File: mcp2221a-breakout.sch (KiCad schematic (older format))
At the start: 27 parts, among them J1 USB_B_Micro, J2 LEFT, J3 RIGHT, U1 MCP1700-3302E, U2 MCP2221AxSL

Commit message: Switch regulator
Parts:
- removed U1: MCP1700-3302E, Package_TO_SOT_SMD:SOT-23, symbol Regulator_Linear:MCP1700-3302E_SOT23
- added U1: MCP1812AT-033_TT, Package_TO_SOT_SMD:SOT-23, symbol mcp2221a-breakout:MCP1812AT-033_TT
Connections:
- net GND: now also U1.3 (GND)
- net VBUS: now also U1.2 (VI)
- net VDD: now also U1.1 (VO)
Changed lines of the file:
@@
-$EndComp
-$Comp
-L Regulator_Linear:MCP1700-3302E_SOT23 U1
-U 1 1 60EED33E
-P 3650 1250
-F 0 "U1" H 3650 1492 50  0000 C CNN
-F 1 "MCP1700-3302E" H 3650 1401 50  0000 C CNN
-F 2 "Package_TO_SOT_SMD:SOT-23" H 3650 1475 50  0001 C CNN
-F 3 "http://ww1.microchip.com/downloads/en/DeviceDoc/20001826D.pdf" H 3650 1250 50  0001 C CNN
-	1    3650 1250
-	1    0    0    -1
 $EndComp
 $Comp
@@
 Wire Notes Line
 	4900 1950 4900 3800
+$Comp
+L mcp2221a-breakout:MCP1812AT-033_TT U1
+U 1 1 60F5FC01
+P 3650 1250
+F 0 "U1" H 3650 1492 50  0000 C CNN
+F 1 "MCP1812AT-033_TT" H 3650 1401 50  0000 C CNN
+F 2 "Package_TO_SOT_SMD:SOT-23" H 3650 1475 50  0001 C CNN
+F 3 "https://www.farnell.com/datasheets/2722379.pdf" H 3650 1250 50  0001 C CNN
+	1    3650 1250
+	1    0    0    -1
+$EndComp
 $EndSCHEMATC

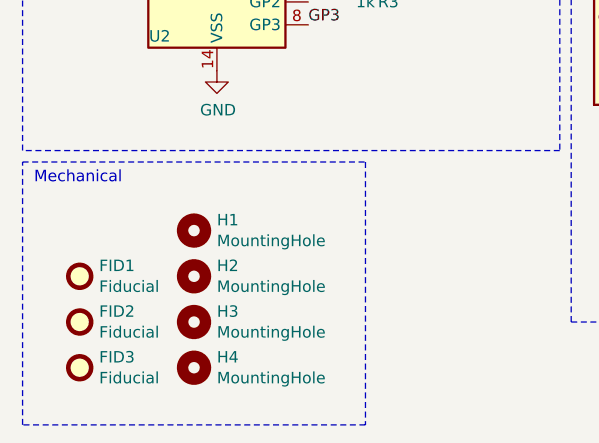
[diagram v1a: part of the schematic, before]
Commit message: Update for KICAD 6.0
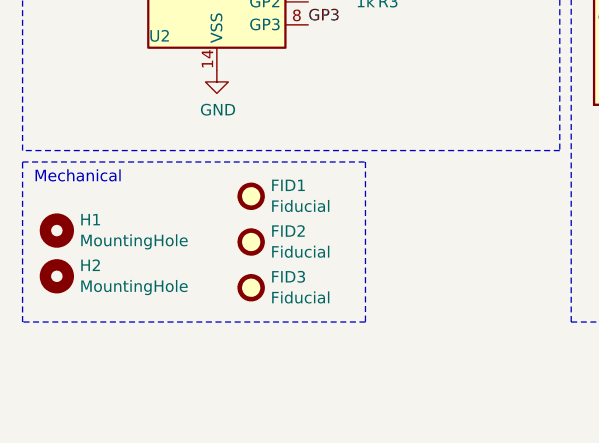
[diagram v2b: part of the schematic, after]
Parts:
- removed H3, H4: MountingHole, MountingHole:MountingHole_2.7mm_M2.5_DIN965_Pad, symbol Mechanical:MountingHole
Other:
- moved on the sheet: FID1, FID2, FID3, H1, H2
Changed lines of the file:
@@
 L Mechanical:Fiducial FID3
 U 1 1 60F19612
-P 750 4000
-F 0 "FID3" H 835 4046 50  0000 L CNN
-F 1 "Fiducial" H 835 3955 50  0000 L CNN
-F 2 "Fiducial:Fiducial_1mm_Mask2mm" H 750 4000 50  0001 C CNN
-F 3 "~" H 750 4000 50  0001 C CNN
-	1    750  4000
-	1    0    0    -1
-$EndComp
-$Comp
-L Mechanical:MountingHole H4
-U 1 1 60F1A4FC
-P 1250 4000
-F 0 "H4" H 1350 4046 50  0000 L CNN
-F 1 "MountingHole" H 1350 3955 50  0000 L CNN
-F 2 "MountingHole:MountingHole_2.7mm_M2.5_DIN965_Pad" H 1250 4000 50  0001 C CNN
-F 3 "~" H 1250 4000 50  0001 C CNN
-	1    1250 4000
+P 1500 3650
+F 0 "FID3" H 1585 3696 50  0000 L CNN
+F 1 "Fiducial" H 1585 3605 50  0000 L CNN
+F 2 "Fiducial:Fiducial_1mm_Mask2mm" H 1500 3650 50  0001 C CNN
+F 3 "~" H 1500 3650 50  0001 C CNN
+	1    1500 3650
 	1    0    0    -1
 $EndComp
@@
 L Mechanical:Fiducial FID2
 U 1 1 60F1ACF7
-P 750 3800
-F 0 "FID2" H 835 3846 50  0000 L CNN
-F 1 "Fiducial" H 835 3755 50  0000 L CNN
-F 2 "Fiducial:Fiducial_1mm_Mask2mm" H 750 3800 50  0001 C CNN
-F 3 "~" H 750 3800 50  0001 C CNN
-	1    750  3800
+P 1500 3450
+F 0 "FID2" H 1585 3496 50  0000 L CNN
+F 1 "Fiducial" H 1585 3405 50  0000 L CNN
+F 2 "Fiducial:Fiducial_1mm_Mask2mm" H 1500 3450 50  0001 C CNN
+F 3 "~" H 1500 3450 50  0001 C CNN
+	1    1500 3450
 	1    0    0    -1
 $EndComp
@@
 L Mechanical:Fiducial FID1
 U 1 1 60F1B0A7
-P 750 3600
-F 0 "FID1" H 835 3646 50  0000 L CNN
-F 1 "Fiducial" H 835 3555 50  0000 L CNN
-F 2 "Fiducial:Fiducial_1mm_Mask2mm" H 750 3600 50  0001 C CNN
-F 3 "~" H 750 3600 50  0001 C CNN
-	1    750  3600
-	1    0    0    -1
-$EndComp
-$Comp
-L Mechanical:MountingHole H3
-U 1 1 60F1B3C8
-P 1250 3800
-F 0 "H3" H 1350 3846 50  0000 L CNN
-F 1 "MountingHole" H 1350 3755 50  0000 L CNN
-F 2 "MountingHole:MountingHole_2.7mm_M2.5_DIN965_Pad" H 1250 3800 50  0001 C CNN
-F 3 "~" H 1250 3800 50  0001 C CNN
-	1    1250 3800
+P 1500 3250
+F 0 "FID1" H 1585 3296 50  0000 L CNN
+F 1 "Fiducial" H 1585 3205 50  0000 L CNN
+F 2 "Fiducial:Fiducial_1mm_Mask2mm" H 1500 3250 50  0001 C CNN
+F 3 "~" H 1500 3250 50  0001 C CNN
+	1    1500 3250
 	1    0    0    -1
 $EndComp
@@
 L Mechanical:MountingHole H2
 U 1 1 60F1B77D
-P 1250 3600
-F 0 "H2" H 1350 3646 50  0000 L CNN
-F 1 "MountingHole" H 1350 3555 50  0000 L CNN
-F 2 "MountingHole:MountingHole_2.7mm_M2.5_DIN965_Pad" H 1250 3600 50  0001 C CNN
-F 3 "~" H 1250 3600 50  0001 C CNN
-	1    1250 3600
+P 650 3600
+F 0 "H2" H 750 3646 50  0000 L CNN
+F 1 "MountingHole" H 750 3555 50  0000 L CNN
+F 2 "MountingHole:MountingHole_2.7mm_M2.5_DIN965_Pad" H 650 3600 50  0001 C CNN
+F 3 "~" H 650 3600 50  0001 C CNN
+	1    650  3600
 	1    0    0    -1
 $EndComp
@@
 L Mechanical:MountingHole H1
 U 1 1 60F1BBEE
-P 1250 3400
-F 0 "H1" H 1350 3446 50  0000 L CNN
-F 1 "MountingHole" H 1350 3355 50  0000 L CNN
-F 2 "MountingHole:MountingHole_2.7mm_M2.5_DIN965_Pad" H 1250 3400 50  0001 C CNN
-F 3 "~" H 1250 3400 50  0001 C CNN
-	1    1250 3400
+P 650 3400
+F 0 "H1" H 750 3446 50  0000 L CNN
+F 1 "MountingHole" H 750 3355 50  0000 L CNN
+F 2 "MountingHole:MountingHole_2.7mm_M2.5_DIN965_Pad" H 650 3400 50  0001 C CNN
+F 3 "~" H 650 3400 50  0001 C CNN
+	1    650  3400
 	1    0    0    -1
 $EndComp
@@
 	500  3100 2000 3100
 Wire Notes Line
-	2000 3100 2000 4250
+	2000 3100 2000 3800
 Wire Notes Line
-	2000 4250 500  4250
+	2000 3800 500  3800
 Wire Notes Line
-	500  4250 500  3100
+	500  3800 500  3100
 Text Notes 550  3200 0    50   ~ 0
 Mechanical
